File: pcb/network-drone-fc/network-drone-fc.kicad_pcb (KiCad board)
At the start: 4 copper layers, 36 x 39 mm, 85 parts, among them J1 U.FL-R-SMT-1, J2 TYPE-C 16PIN 2MD, J3 U.FL GPS, J4 ESC, J5 Sensor port 5V I2C, J6 Radio UART 5V, J7 Charging board, J8 Landing sensor 5V I2C, U1 ESP32-S3FN8, U2 USBLC6-2SC6, U3 AP63205WU-7, U4 TLV75733PDRVR, U5 TPS7A2033PDBVR, U6 ICM-42688-P, U7 BMP581, U8 MAX-M10S, X1 Q22FA12800101

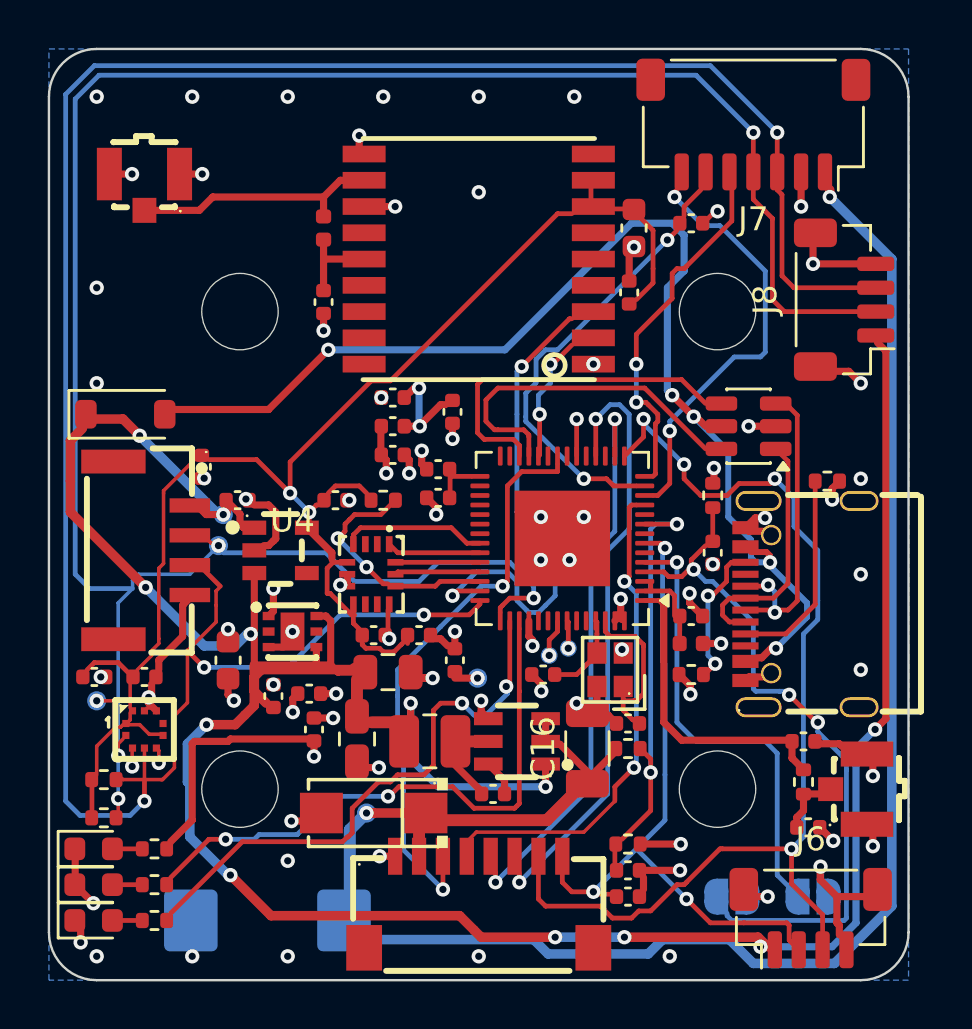
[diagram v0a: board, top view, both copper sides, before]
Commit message: PCB: long diagonal tracks straightened into horizontal and vertical runs
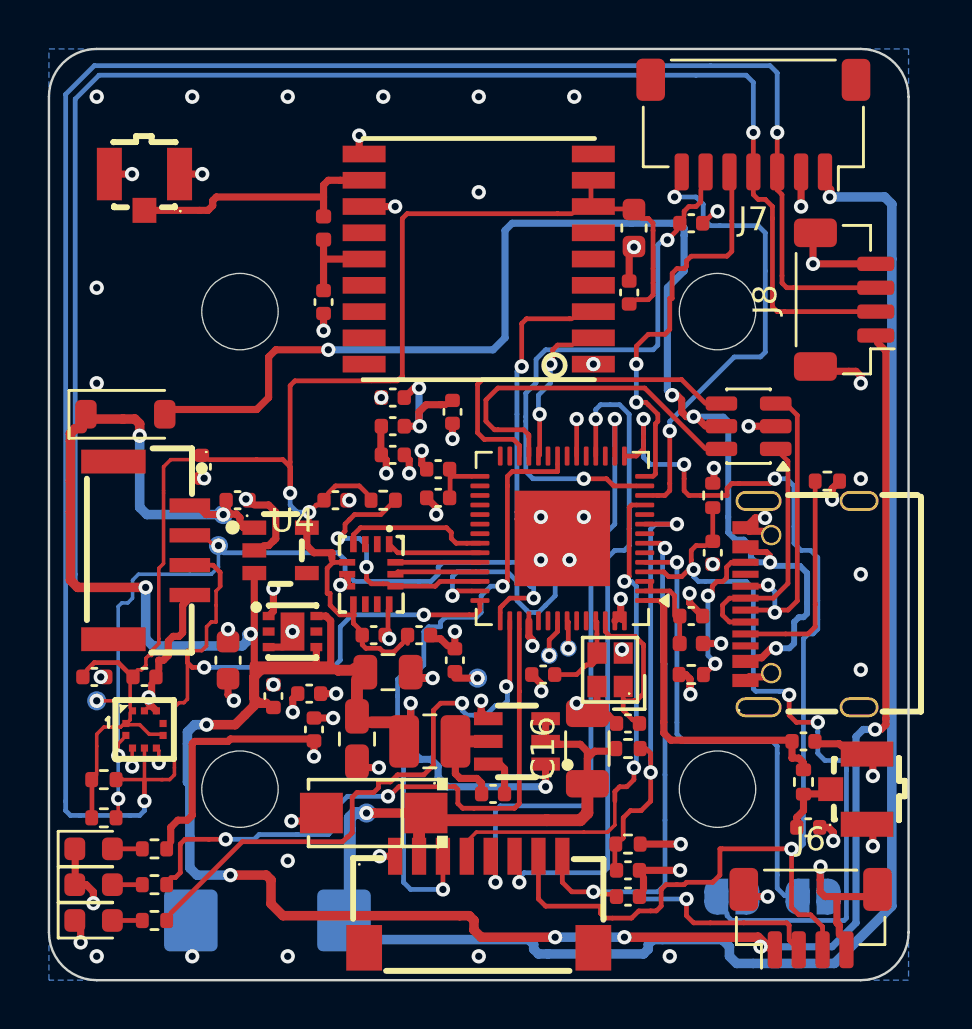
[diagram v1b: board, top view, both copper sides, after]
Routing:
- net +3V3_SENS: track 59.8 -> 68.7 mm
- net +5V: track 118.6 -> 126.6 mm
- net VBUS: track 48.5 -> 54.7 mm
- net I2C_SDA: track 102.1 -> 106.6 mm
- net VBAT: track 75.4 -> 79.3 mm
- net ESC_TELEM: track 44.2 -> 48.1 mm
- net CHG_STAT: track 18.0 -> 21.9 mm
- net I2C_SCL: track 94.6 -> 97.9 mm
- net MOTOR4: track 25.3 -> 27.7 mm
- net MOTOR3: track 23.4 -> 25.8 mm
- net Net-(JP1-B): track 27.6 -> 29.7 mm
- net MOTOR1: track 23.5 -> 25.6 mm
- net GPS_TX: track 20.3 -> 22.4 mm
- net GND: track 66.1 -> 67.8 mm
- net Green: track 23.9 -> 25.4 mm
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
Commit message: Part values: SMAJ12A surge diode, 16 V buck output capacitors, crystal and diode labels match the parts ordered
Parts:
- C18, C19: value 22uF 10V -> 22uF 16V
- D1: value B5819W -> 1N5819HW
- D5: value SMAJ18A -> SMAJ12A
- X1: value Q22FA12800101 -> FA-128 40MHz 10pF
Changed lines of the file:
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@@
 			)
 		)
-		(property "Value" "SMAJ18A"
+		(property "Value" "SMAJ12A"
 			(at 0 4 180)
 			(layer "F.Fab")
@@
 			)
 		)
-		(property "Value" "22uF 10V"
+		(property "Value" "22uF 16V"
 			(at 0 1.68 270)
 			(layer "F.Fab")
@@
 			)
 		)
-		(property "Value" "22uF 10V"
+		(property "Value" "22uF 16V"
 			(at 0 1.68 0)
 			(layer "F.Fab")
@@
 			)
 		)
-		(property "Value" "B5819W"
+		(property "Value" "1N5819HW"
 			(at 0 2.1 0)
 			(layer "F.Fab")
@@
 			)
 		)
-		(property "Value" "Q22FA12800101"
+		(property "Value" "FA-128 40MHz 10pF"
 			(at 0 4.55 90)
 			(layer "F.Fab")

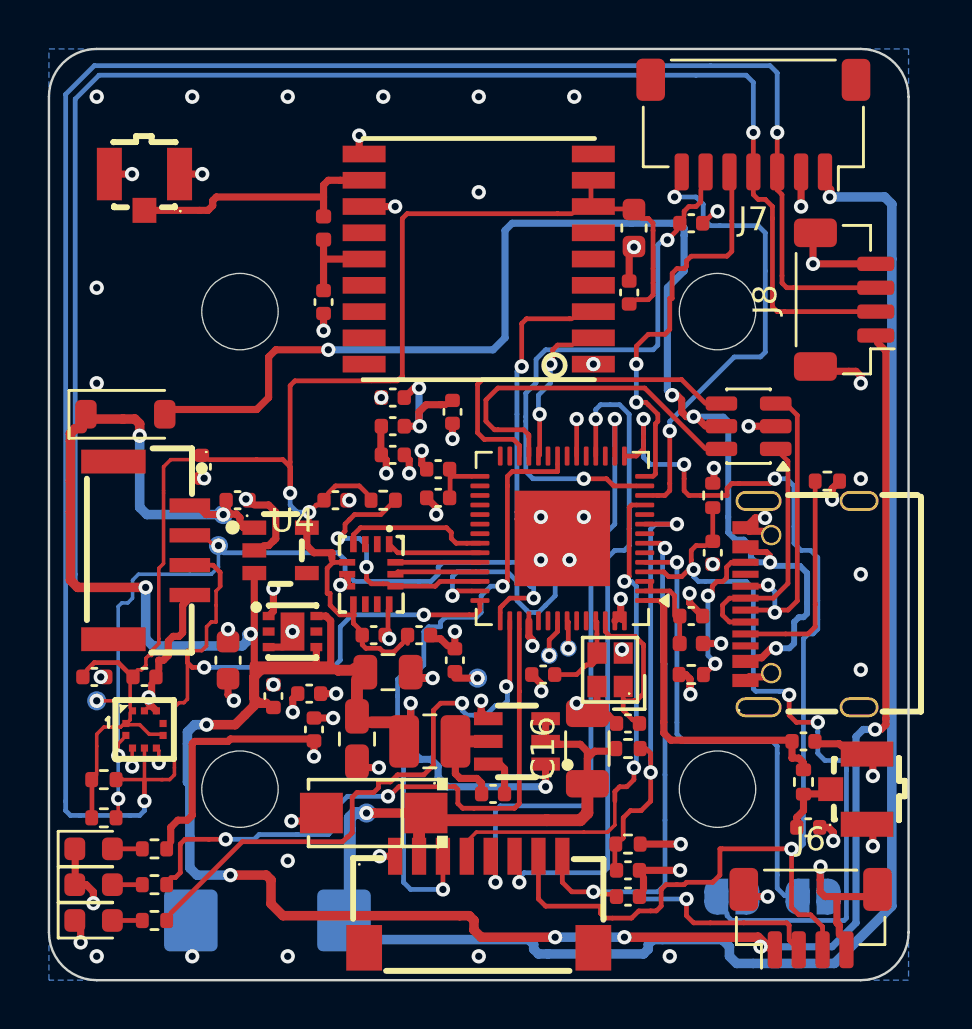
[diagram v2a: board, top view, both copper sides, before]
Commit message: PCB: VBUS capacitor and boot pull-up on the bottom, antenna socket vias moved out from under J1 and J3, USB-C tab pads enlarged
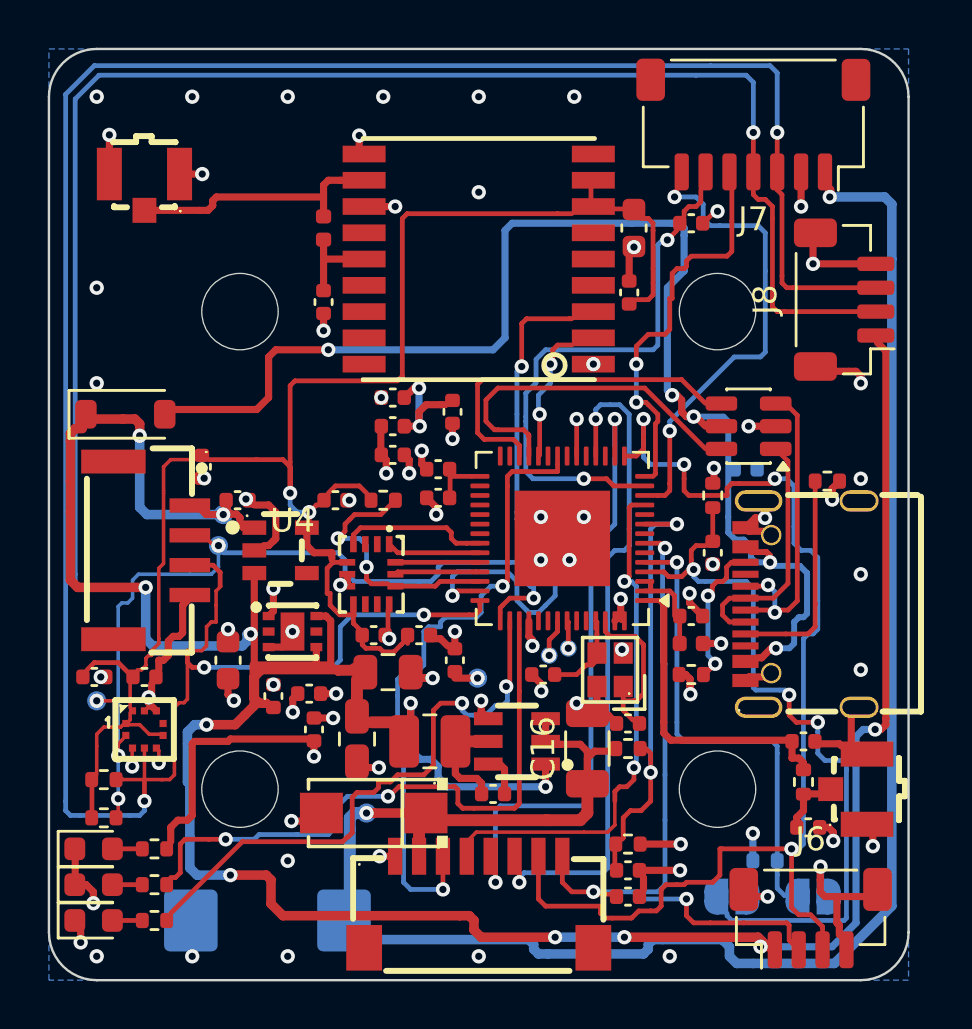
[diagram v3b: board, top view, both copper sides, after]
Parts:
- added C36: 100nF, Capacitor_SMD:C_0402_1005Metric, B.Cu at (111.2, 96.6)
- added R16: 10k, Resistor_SMD:R_0402_1005Metric, B.Cu at (112.0, 113.0)
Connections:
- net Net-(JP2-B) renamed BOOT
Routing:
- net +3V3: track 21.0 -> 22.2 mm, vias 13 -> 14
- net GND: vias 76 -> 75

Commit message: Battery cut-off on the 5 V regulator's enable pin
R14 143k and R15 34k on the bottom set the AP63205 to turn on at about
5.9 V and off at about 4.9 V. C16 is now 0805 so the battery reaches VIN
through its own channel, and the green LED track moves left under the
regulator to make room for the enable via.
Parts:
- added R14: 143k, Resistor_SMD:R_0402_1005Metric, B.Cu at (103.7, 108.5)
- added R15: 34k, Resistor_SMD:R_0402_1005Metric, B.Cu at (101.8, 106.9)
- C16: footprint Capacitor_SMD:C_1206_3216Metric -> Capacitor_SMD:C_0805_2012Metric
- moved C16 0.20 mm to (104.8, 108.3)
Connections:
- U3 pad 2: VBAT -> BUCK_EN
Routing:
- net BUCK_EN: track 0.00 -> 3.39 mm, vias 0 -> 1
- net GND: track 67.8 -> 69.8 mm
- net Green: track 25.4 -> 26.0 mm
- net VBAT: track 79.3 -> 79.1 mm, vias 2 -> 3

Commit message: ESP32 supply capacitors at the pins' plane vias
C37 (1 uF) on the VDDA pins 55 and 56, C38 (0.1 uF) on VDD3P3_CPU and
C39 (0.1 uF) on VDD3P3_RTC, all on the bottom directly under each pin's
via. The nearest capacitors before were 4 to 7 mm away.
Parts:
- added C37: 1uF, Capacitor_SMD:C_0402_1005Metric, B.Cu at (106.0, 103.1)
- added C38: 0.1uF, Capacitor_SMD:C_0402_1005Metric, B.Cu at (101.3, 104.0)
- added C39: 0.1uF, Capacitor_SMD:C_0402_1005Metric, B.Cu at (103.5, 95.2)
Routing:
- net +3V3: track 22.2 -> 23.8 mm
- net GND: track 69.8 -> 70.4 mm

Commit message: 24 nH series inductor on the crystal's XTAL_P line
Espressif's hardware design guide asks for a series part on XTAL_P,
starting at 24 nH, to keep the crystal's harmonics out of the radio. L4
sits in the existing vertical run beside the crystal. The chip side of
the line is now the net XTAL_P_CHIP.

The schematic symbols for R14, R15 and C37 to C39 also move out of the
title block and a text note into empty space, with their labels drawn
the right way round.
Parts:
- added L4: 24nH, Inductor_SMD:L_0402_1005Metric, F.Cu at (107.0, 105.0)
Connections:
- U1 pad 54: XTAL_P -> XTAL_P_CHIP
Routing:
- net XTAL_P: track 6.92 -> 3.11 mm
- net XTAL_P_CHIP: track 0.00 -> 2.85 mm
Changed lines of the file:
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@@
 	(net 94 "unconnected-(J7-Pad9)")
 	(net 95 "BUCK_EN")
+	(net 96 "XTAL_P_CHIP")
 	(footprint "MountingHole:MountingHole_3.2mm_M3"
 		(layer "F.Cu")
@@
 		)
 	)
+	(footprint "Inductor_SMD:L_0402_1005Metric"
+		(layer "F.Cu")
+		(at 106.95 105 -90)
+		(descr "Inductor SMD 0402 (1005 Metric), square (rectangular) end terminal, IPC-7351 nominal, (Body size source: http://www.tortai-tech.com/upload/download/2011102023233369053.pdf), generated with kicad-footprint-generator")
+		(tags "inductor")
+		(property "Reference" "L4"
+			(at 0 -1.17 270)
+			(layer "F.SilkS")
+			(hide yes)
+			(effects
+				(font
+					(size 1 1)
+					(thickness 0.15)
+				)
+			)
+		)
+		(property "Value" "24nH"
+			(at 0 1.17 270)
+			(layer "F.Fab")
+			(effects
+				(font
+					(size 1 1)
+					(thickness 0.15)
+				)
+			)
+		)
+		(property "Datasheet" ""
+			(at 0 0 270)
+			(layer "F.Fab")
+			(hide yes)
+			(effects
+				(font
+					(size 1.27 1.27)
+					(thickness 0.15)
+				)
+			)
+		)
+		(property "Description" ""
+			(at 0 0 270)
+			(layer "F.Fab")
+			(hide yes)
+			(effects
+				(font
+					(size 1.27 1.27)
+					(thickness 0.15)
+				)
+			)
+		)
+		(attr smd)
+		(fp_rect
+			(start -0.93 -0.47)
+			(end 0.93 0.47)
+			(stroke
+				(width 0.05)
+				(type solid)
+			)
+			(fill no)
+			(layer "F.CrtYd")
+		)
+		(fp_rect
+			(start -0.5 -0.25)
+			(end 0.5 0.25)
+			(stroke
+				(width 0.1)
+				(type solid)
+			)
+			(fill no)
+			(layer "F.Fab")
+		)
+		(fp_text user "${REFERENCE}"
+			(at 0 0 270)
+			(layer "F.Fab")
+			(effects
+				(font
+					(size 0.25 0.25)
+					(thickness 0.04)
+				)
+			)
+		)
+		(pad "1" smd roundrect
+			(at -0.485 0 270)
+			(size 0.59 0.64)
+			(layers "F.Cu" "F.Mask" "F.Paste")
+			(roundrect_rratio 0.25)
+			(net 96 "XTAL_P_CHIP")
+		)
+		(pad "2" smd roundrect
+			(at 0.485 0 270)
+			(size 0.59 0.64)
+			(layers "F.Cu" "F.Mask" "F.Paste")
+			(roundrect_rratio 0.25)
+			(net 42 "XTAL_P")
+		)
+		(embedded_fonts no)
+		(model "${KICAD9_3DMODEL_DIR}/Inductor_SMD.3dshapes/L_0402_1005Metric.step"
+			(offset
+				(xyz 0 0 0)
+			)
+			(scale
+				(xyz 1 1 1)
+			)
+			(rotate
+				(xyz 0 0 0)
+			)
+		)
+	)
 	(footprint "Resistor_SMD:R_0402_1005Metric"
 		(layer "F.Cu")
@@
 			(layers "F.Cu" "F.Mask" "F.Paste")
 			(roundrect_rratio 0.25)
-			(net 42 "XTAL_P")
+			(net 96 "XTAL_P_CHIP")
 		)
 		(pad "55" smd roundrect
@@
 	)
 	(gr_text "TAR Team 1  network drone FC  rev A"
-		(at 100 94 0)
+		(at 100 93.5 0)
 		(layer "B.SilkS")
 		(effects
@@
 	)
 	(segment
-		(start 106.05 106.7)
-		(end 106.45 107.1)
+		(start 106.9 105.48)
+		(end 106.9 106)
 		(width 0.2)
 		(layer "F.Cu")
@@
 	)
 	(segment
-		(start 105.3 102.95)
-		(end 105.3 103.399999)
+		(start 106.05 106.7)
+		(end 106.45 107.1)
 		(width 0.2)
 		(layer "F.Cu")
@@
 	)
 	(segment
-		(start 106.9 103.95)
-		(end 106.55 103.6)
-		(width 0.2)
-		(layer "F.Cu")
-		(net 42)
-	)
-	(segment
-		(start 106.9 104)
-		(end 106.9 106)
-		(width 0.2)
-		(layer "F.Cu")
-		(net 42)
-	)
-	(segment
-		(start 105.5 103.6)
-		(end 106.55 103.6)
-		(width 0.2)
-		(layer "F.Cu")
-		(net 42)
-	)
-	(segment
 		(start 106.9 106)
 		(end 106.6 106.3)
@@
 	)
 	(segment
-		(start 106.9 104)
-		(end 106.9 103.95)
-		(width 0.2)
-		(layer "F.Cu")
-		(net 42)
-	)
-	(segment
 		(start 106.05 106.3)
 		(end 106.05 105.7)
@@
 	)
 	(segment
-		(start 105.3 103.399999)
-		(end 105.5 103.6)
-		(width 0.2)
-		(layer "F.Cu")
-		(net 42)
-	)
-	(segment
 		(start 106.5 106.3)
 		(end 106.05 106.3)
@@
 		(net 95)
 	)
+	(segment
+		(start 106.9 104)
+		(end 106.9 104.52)
+		(width 0.2)
+		(layer "F.Cu")
+		(net 96)
+	)
+	(segment
+		(start 105.3 102.95)
+		(end 105.3 103.399999)
+		(width 0.2)
+		(layer "F.Cu")
+		(net 96)
+	)
+	(segment
+		(start 106.9 103.95)
+		(end 106.55 103.6)
+		(width 0.2)
+		(layer "F.Cu")
+		(net 96)
+	)
+	(segment
+		(start 105.5 103.6)
+		(end 106.55 103.6)
+		(width 0.2)
+		(layer "F.Cu")
+		(net 96)
+	)
+	(segment
+		(start 106.9 104)
+		(end 106.9 103.95)
+		(width 0.2)
+		(layer "F.Cu")
+		(net 96)
+	)
+	(segment
+		(start 105.3 103.399999)
+		(end 105.5 103.6)
+		(width 0.2)
+		(layer "F.Cu")
+		(net 96)
+	)
 	(zone
